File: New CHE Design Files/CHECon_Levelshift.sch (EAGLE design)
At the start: 42 parts, among them U2 MAX232SOIC16, U3 RS485SOIC

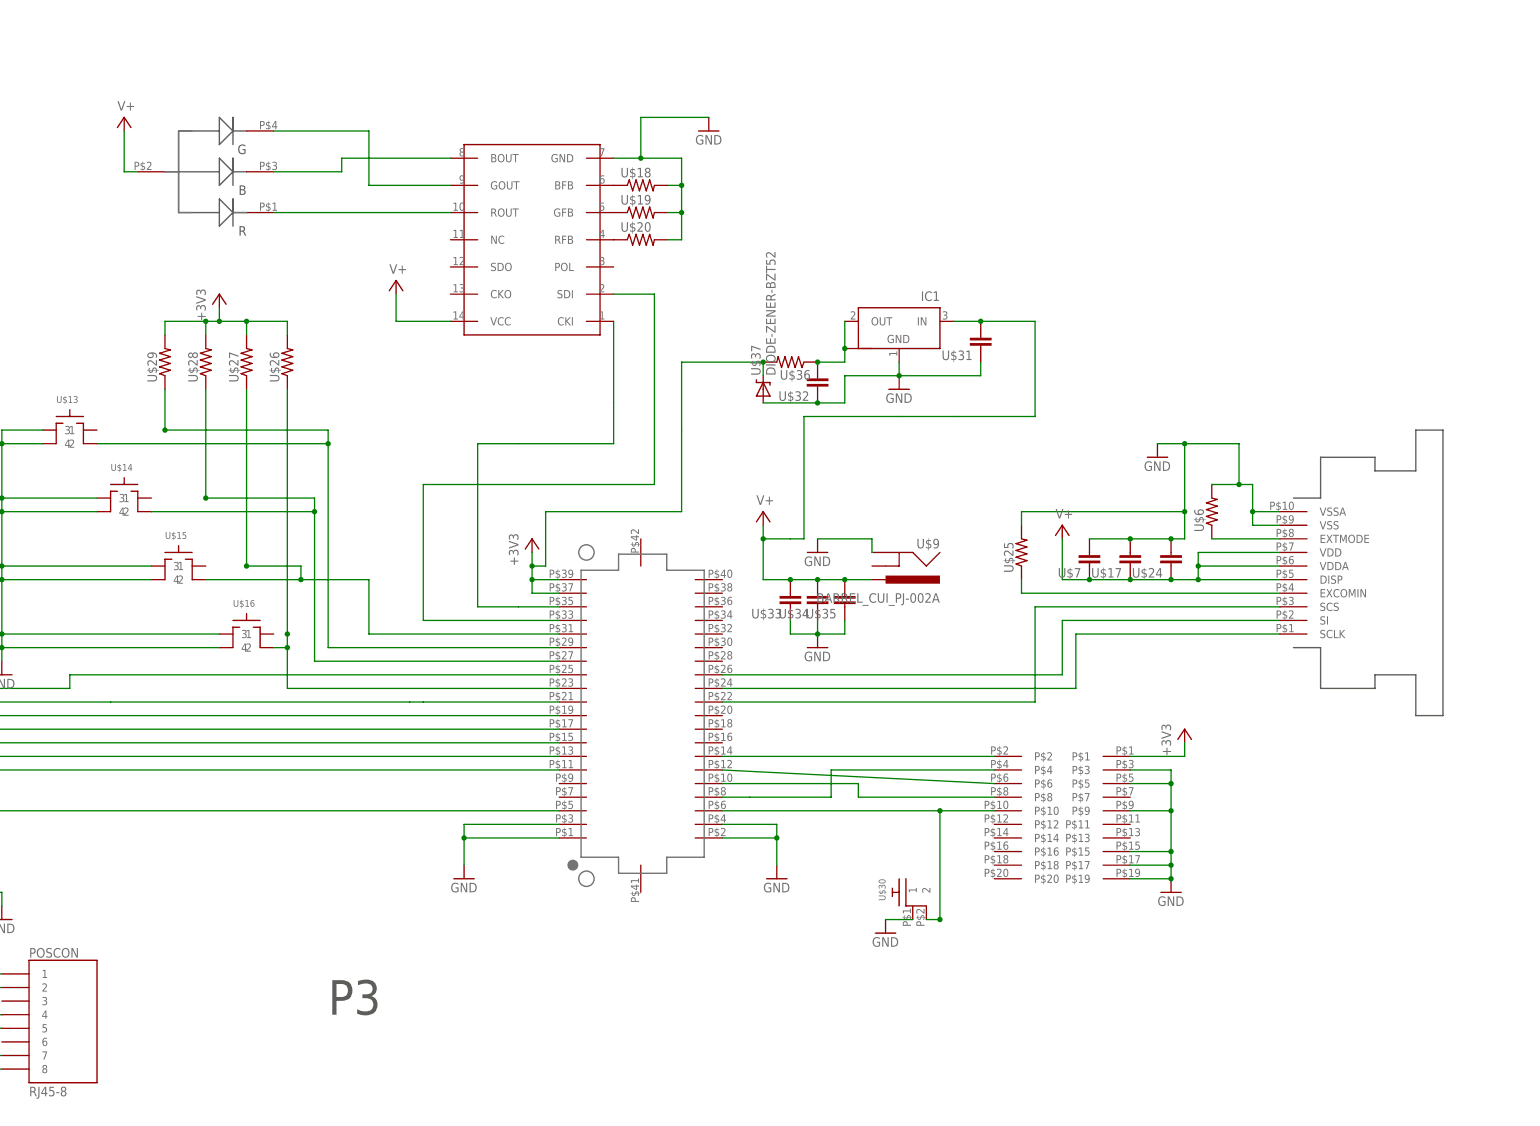
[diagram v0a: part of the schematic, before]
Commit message: P3
Added VR and Zener just in case
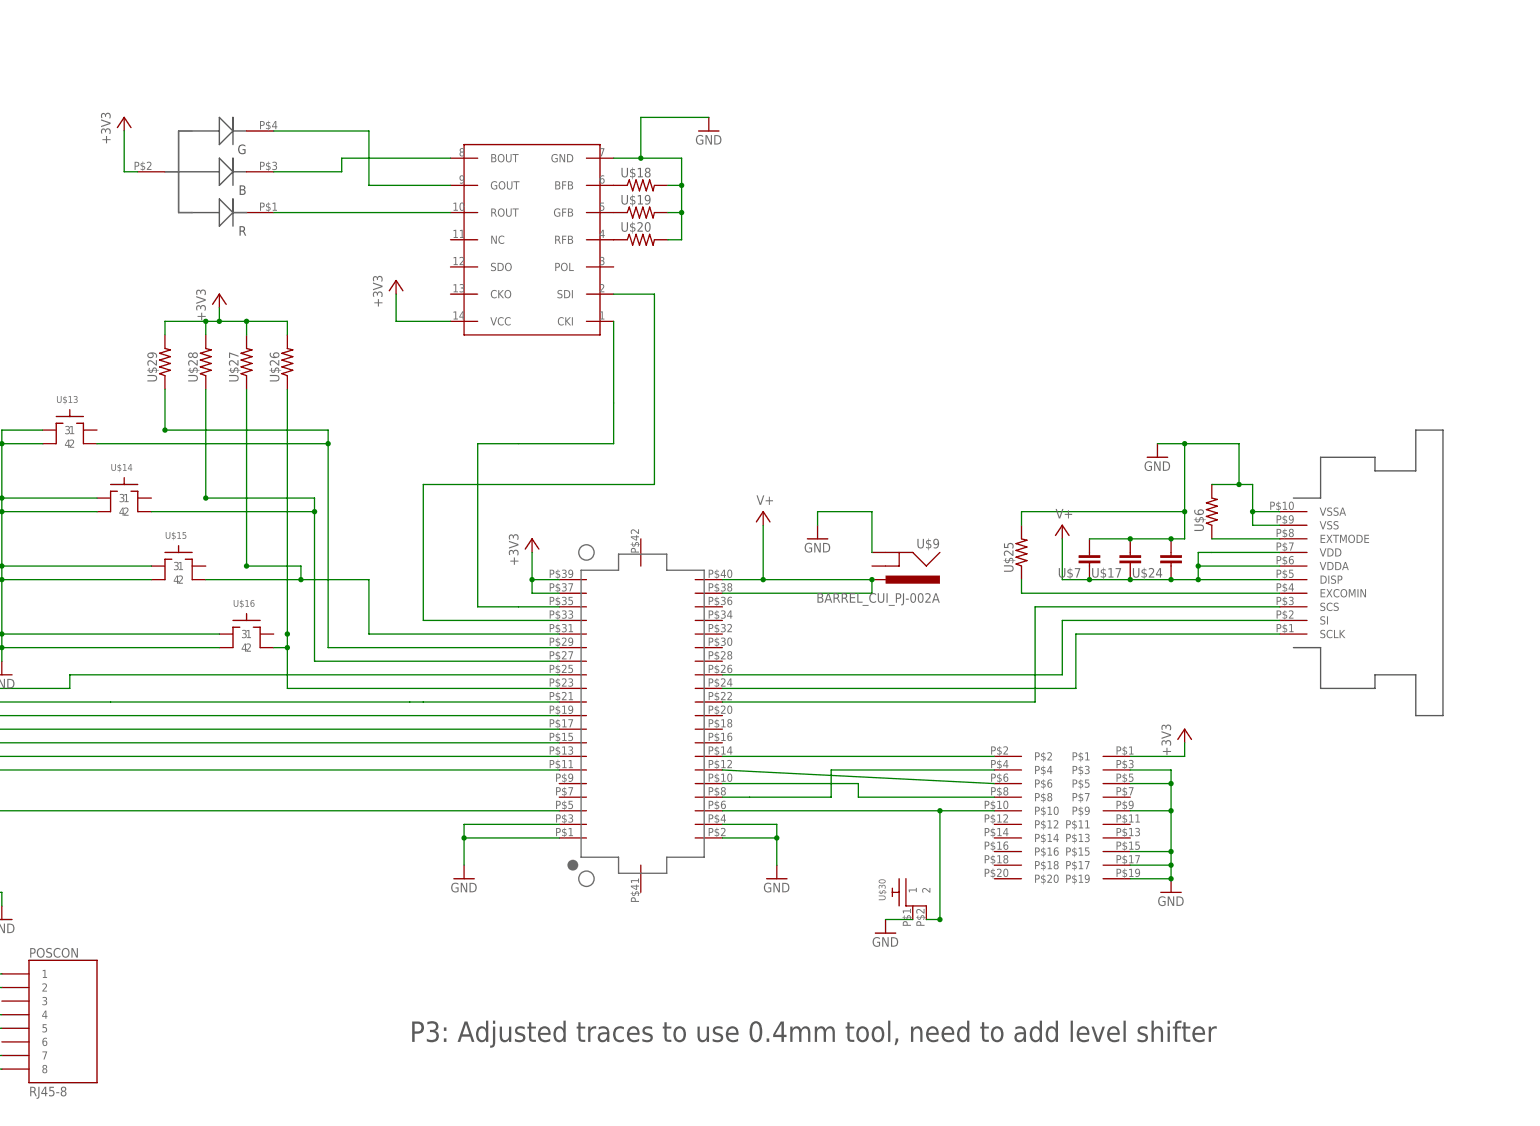
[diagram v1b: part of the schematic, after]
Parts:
- removed IC1: (no value), KW2:NCP1117ST33T3G_1
- removed U$31, U$32, U$33, U$34, U$35: (no value), GW-devices:RF-C0805
- removed U$36: (no value), GW-devices:RF-R0805
- removed U$37: DIODE-ZENER-BZT52, SparkFun:DIODE-ZENER-BZT52
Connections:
- removed net OUT1: IC1.OUT, IC1.OUT1, U$32.2, U$36.1
- net +3V3: now also U$1.ANODE, U$8.VCC; no longer U$36.2, U$37.C
- net GND: no longer IC1.GND, U$31.1, U$32.1, U$33.1, U$34.1, U$35.1, U$37.A
- net V+: now also U$10.VIN@1, U$10.VIN@2; no longer IC1.IN, U$1.ANODE, U$31.2, U$33.2, U$34.2, U$35.2, U$8.VCC
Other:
- note added: "P3: Adjusted traces to use 0.4mm tool, need to add level shifter"
- note removed: "P3"
